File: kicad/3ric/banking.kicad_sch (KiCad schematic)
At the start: 10 parts, among them CON2 SJ-3523-SMT-TR

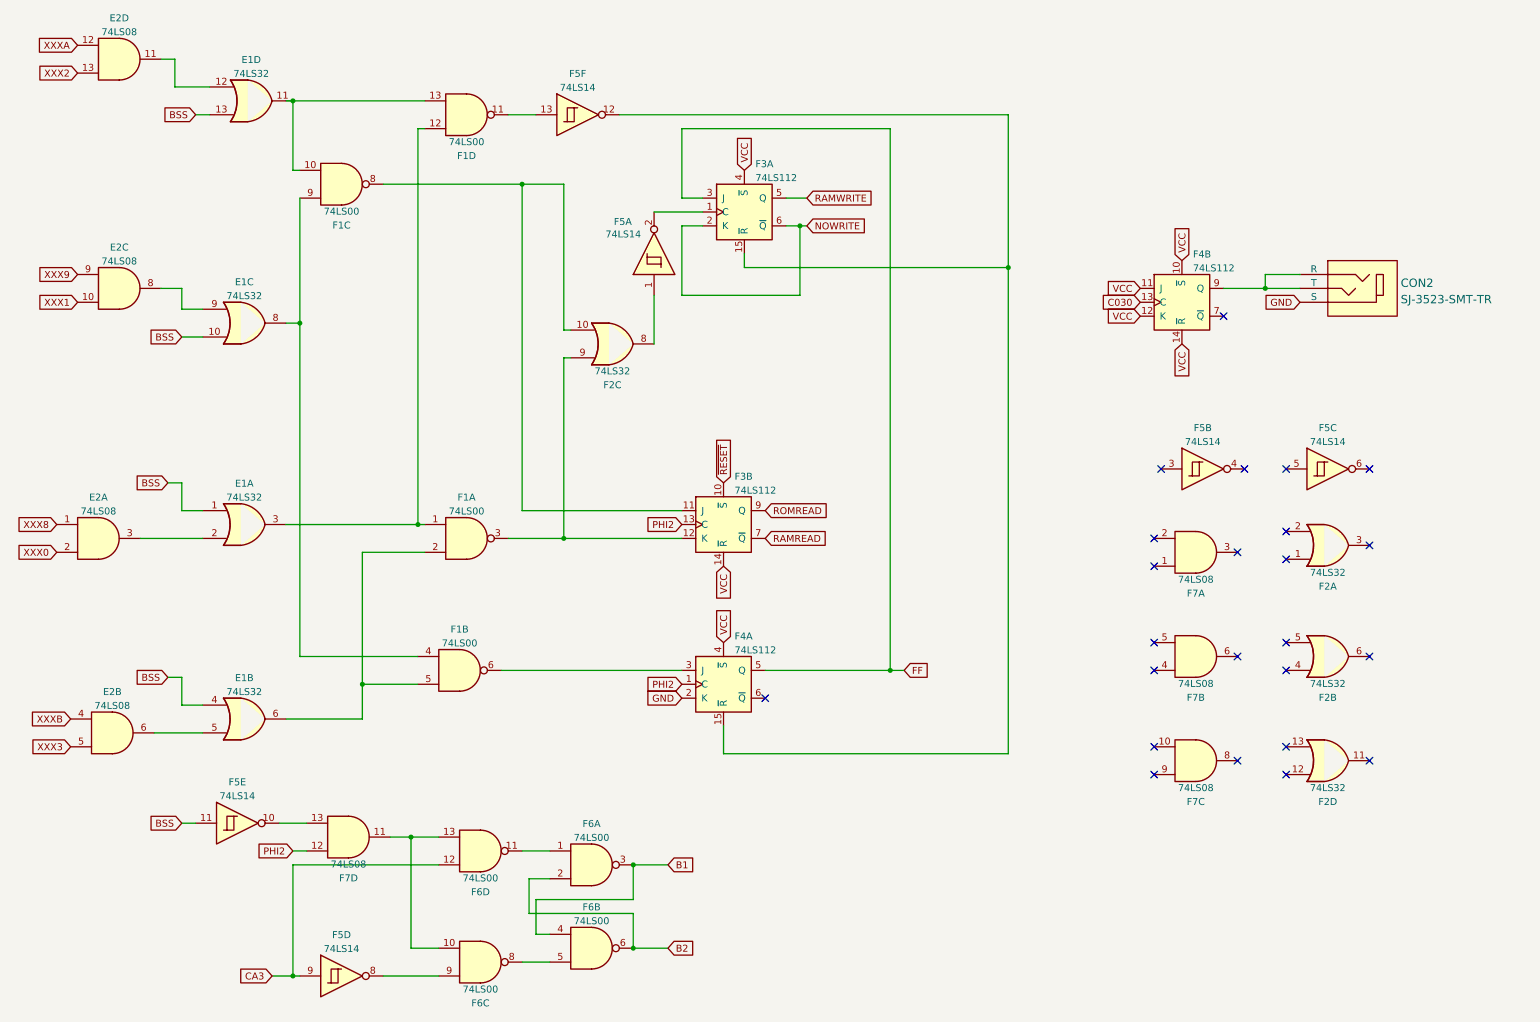
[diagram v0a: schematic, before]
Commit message: updated schematics and PCB PNG of the breadboard layout
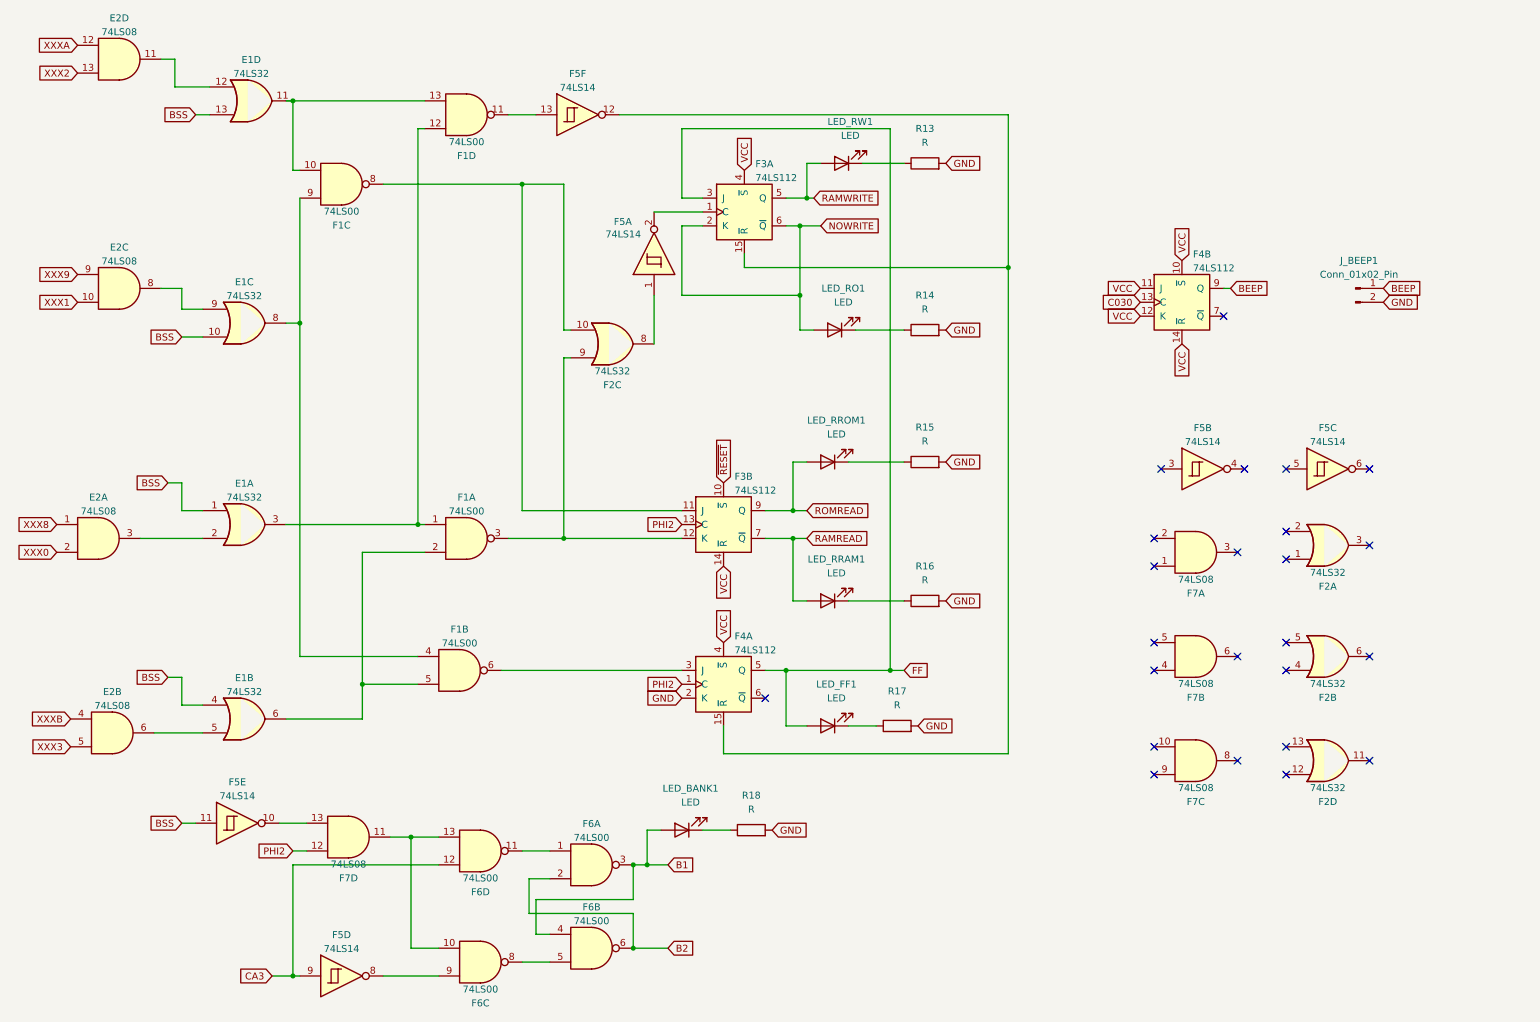
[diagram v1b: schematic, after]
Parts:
- removed CON2: SJ-3523-SMT-TR, digikey-footprints:Switch_Slide_11.6x4mm_SJ-3523-SMT, symbol dk_Barrel-Audio-Connectors:SJ-3523-SMT-TR
- added J_BEEP1: Conn_01x02_Pin, Connector_PinHeader_2.54mm:PinHeader_2x01_P2.54mm_Vertical, symbol Connector:Conn_01x02_Pin
- added LED_BANK1, LED_FF1, LED_RO1, LED_RRAM1, LED_RROM1, LED_RW1: LED, LED_THT:LED_D5.0mm, symbol Device:LED
- added R13, R14, R15, R16, R17, R18: R, Resistor_SMD:R_0603_1608Metric_Pad0.98x0.95mm_HandSolder, symbol Device:R
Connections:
- net B1: now also LED_BANK1.2 (A)
- net FF: now also LED_FF1.2 (A)
- net GND: now also J_BEEP1.2 (Pin_2), R13.2, R14.2, R15.2, R16.2, R17.2, R18.2
- net NOWRITE: now also LED_RO1.2 (A)
- net RAMREAD: now also LED_RRAM1.2 (A)
- net RAMWRITE: now also LED_RW1.2 (A)
- net ROMREAD: now also LED_RROM1.2 (A)
- net BEEP: now reaches F4.9 (Q)
- net BEEP: now also J_BEEP1.1 (Pin_1)
- new net: LED_RO1.1 (K), R14.1
- new net: LED_RRAM1.1 (K), R16.1
- new net: LED_RW1.1 (K), R13.1
- new net: LED_FF1.1 (K), R17.1
- new net: LED_BANK1.1 (K), R18.1
- new net: LED_RROM1.1 (K), R15.1

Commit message: pcb layout continued
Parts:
- removed J_BEEP1: Conn_01x02_Pin, Connector_PinHeader_2.54mm:PinHeader_2x01_P2.54mm_Vertical, symbol Connector:Conn_01x02_Pin
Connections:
- net B1 renamed BANK1
- net B2 renamed BANK2
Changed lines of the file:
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@@
 		)
 	)
-	(global_label "B1"
+	(global_label "BANK1"
 		(shape input)
 		(at 139.7 171.45 0)
@@
 		)
 		(property "Intersheetrefs" "${INTERSHEET_REFS}"
-			(at 144.5926 171.3706 0)
+			(at 148.8538 171.45 0)
 			(effects
 				(font
@@
 		)
 	)
-	(global_label "GND"
-		(shape input)
-		(at 270.51 68.58 0)
-		(fields_autoplaced yes)
-		(effects
-			(font
-				(size 1.27 1.27)
-			)
-			(justify left)
-		)
-		(property "Intersheetrefs" "${INTERSHEET_REFS}"
-			(at 276.7936 68.5006 0)
-			(effects
-				(font
-					(size 1.27 1.27)
-				)
-				(justify left)
-				(hide yes)
-			)
-		)
-	)
 	(global_label "PHI2"
 		(shape input)
@@
 		)
 	)
-	(global_label "BEEP"
-		(shape input)
-		(at 270.51 66.04 0)
-		(fields_autoplaced yes)
-		(effects
-			(font
-				(size 1.27 1.27)
-			)
-			(justify left)
-		)
-		(property "Intersheetrefs" "${INTERSHEET_REFS}"
-			(at 278.3332 66.04 0)
-			(effects
-				(font
-					(size 1.27 1.27)
-				)
-				(justify left)
-				(hide yes)
-			)
-		)
-	)
 	(global_label "~{RESET}"
 		(shape input)
@@
 		)
 	)
-	(global_label "B2"
+	(global_label "BANK2"
 		(shape input)
 		(at 139.7 186.69 0)
@@
 		)
 		(property "Intersheetrefs" "${INTERSHEET_REFS}"
-			(at 144.5926 186.6106 0)
+			(at 148.8538 186.69 0)
 			(effects
 				(font
@@
 				)
 			)
-		)
-	)
-	(symbol
-		(lib_id "Connector:Conn_01x02_Pin")
-		(at 265.43 66.04 0)
-		(unit 1)
-		(exclude_from_sim no)
-		(in_bom yes)
-		(on_board yes)
-		(dnp no)
-		(fields_autoplaced yes)
-		(property "Reference" "J_BEEP1"
-			(at 266.065 60.96 0)
-			(effects
-				(font
-					(size 1.27 1.27)
-				)
-			)
-		)
-		(property "Value" "Conn_01x02_Pin"
-			(at 266.065 63.5 0)
-			(effects
-				(font
-					(size 1.27 1.27)
-				)
-			)
-		)
-		(property "Footprint" "Connector_PinHeader_2.54mm:PinHeader_2x01_P2.54mm_Vertical"
-			(at 265.43 66.04 0)
-			(effects
-				(font
-					(size 1.27 1.27)
-				)
-				(hide yes)
-			)
-		)
-		(property "Datasheet" "~"
-			(at 265.43 66.04 0)
-			(effects
-				(font
-					(size 1.27 1.27)
-				)
-				(hide yes)
-			)
-		)
-		(property "Description" "Generic connector, single row, 01x02, script generated"
-			(at 265.43 66.04 0)
-			(effects
-				(font
-					(size 1.27 1.27)
-				)
-				(hide yes)
-			)
-		)
-		(pin "2"
-		)
-		(pin "1"
-		)
-		(instances
-			(project ""
-				(path "/e63e39d7-6ac0-4ffd-8aa3-1841a4541b55/c920751f-edd2-4cd3-a630-9d0b3423e6d7"
-					(reference "J_BEEP1")
-					(unit 1)
-				)
-			)

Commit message: v2 pcb
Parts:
- removed F7: 74LS08, Package_DIP:DIP-14_W7.62mm_Socket, symbol 74xx:74LS08
- added C5: 74LS08, Package_DIP:DIP-14_W7.62mm_Socket, symbol 74xx:74LS08
- R13, R14, R15, R16, R17, R18: value R -> R220
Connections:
- net BANK1: no longer LED_BANK1.2 (A)
- net BANK2: now also LED_BANK1.2 (A)
- net PHI2: now also C5.2
- net at F6.10, F6.13: now also C5.3
- net at F5.10: now also C5.1
- no-connect marks 24 -> 15
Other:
- moved on the sheet: LED_BANK1, R18
